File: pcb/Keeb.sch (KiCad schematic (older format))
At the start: 43 parts, among them J1 TRRS_SJ1-42514, J2 TRRS_SJ1-42514, SW1 SW_RST, U1 ATMEGA32U4, U2 PI6ULS5V9511AWEX_I2C_HotSwap, U3 MCP23017_SO, X1 XTAL_GND

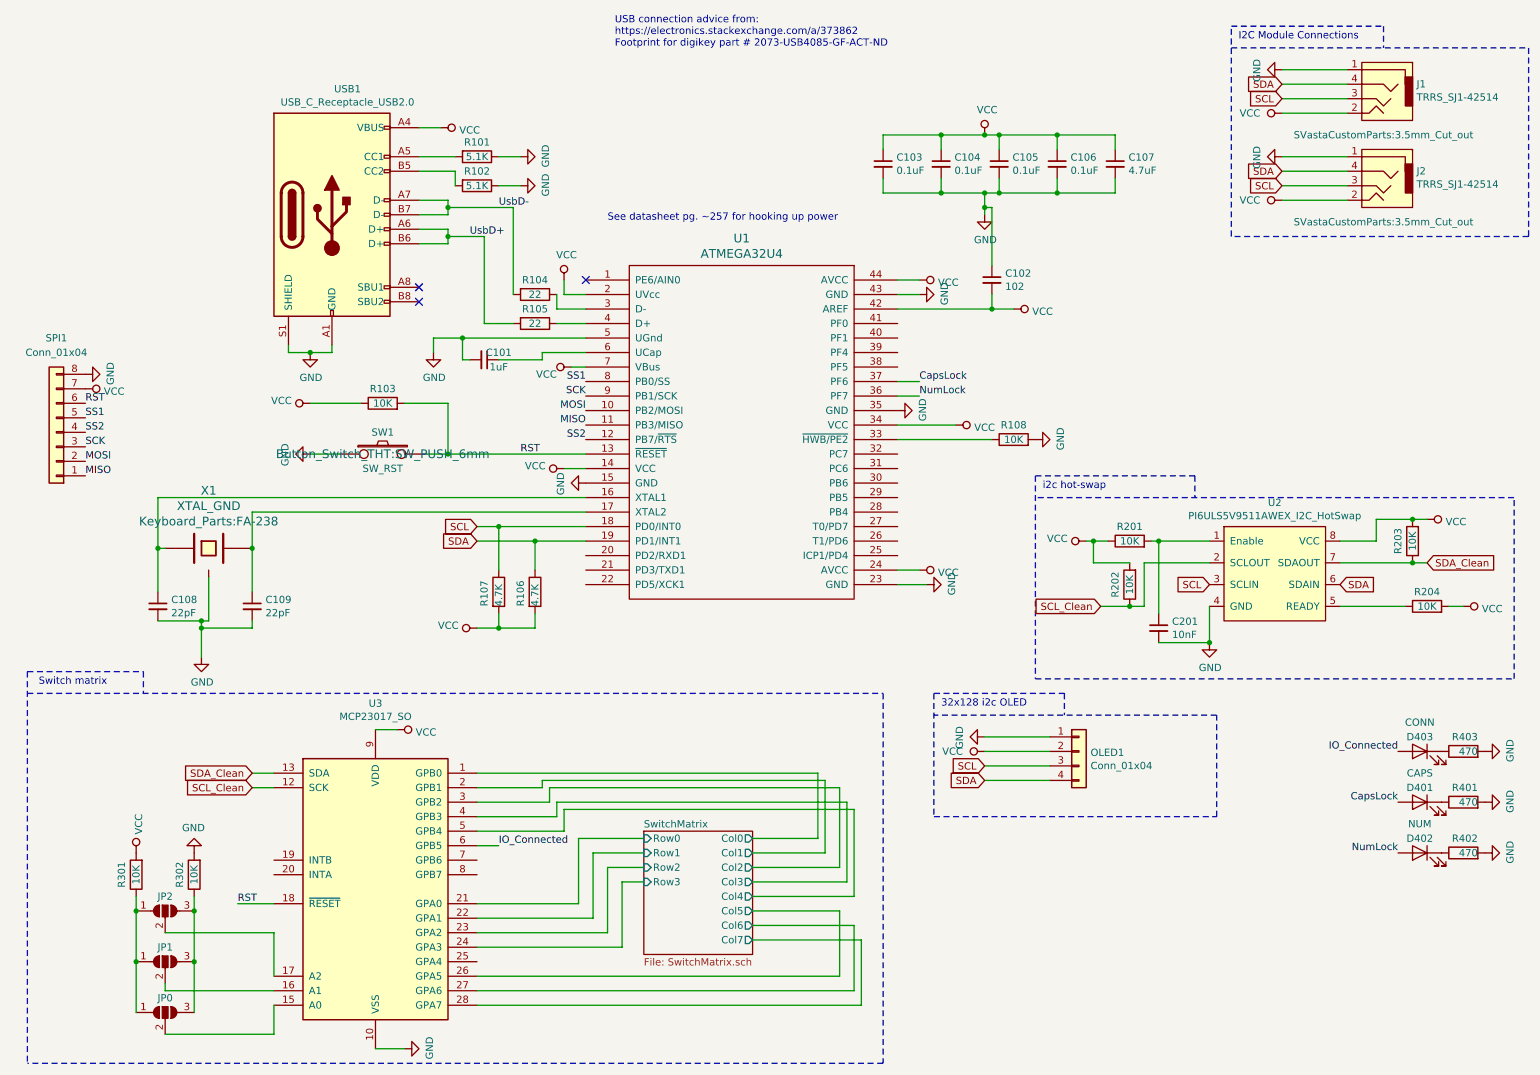
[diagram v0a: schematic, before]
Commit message: Removed most keys to prepare for test PCB
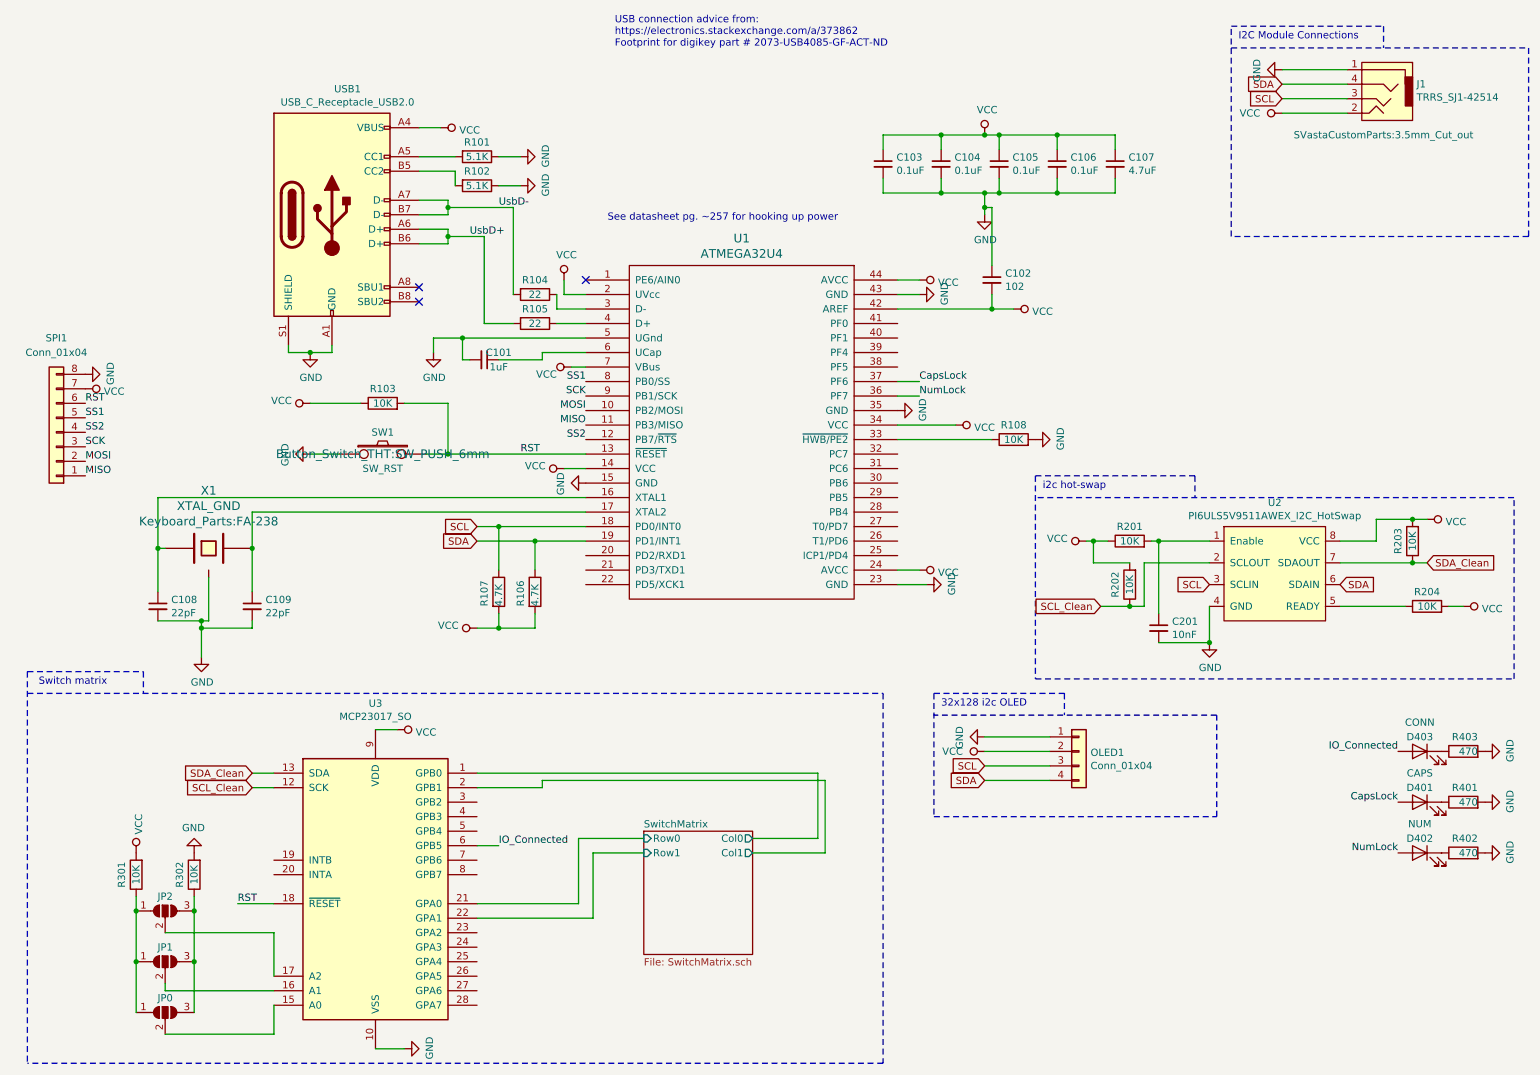
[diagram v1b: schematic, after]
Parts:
- removed J2: TRRS_SJ1-42514, SVastaCustomParts:3.5mm_Cut_out, symbol Keeb-rescue:TRRS_SJ1-42514-SVastaCustomParts-Keeb-rescue
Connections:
- net SwitchMatrix/Col2: no longer names the net of U3.3 (GPB2)
- net SwitchMatrix/Col3: no longer names the net of U3.4 (GPB3)
- net SwitchMatrix/Col4: no longer names the net of U3.5 (GPB4)
- net SwitchMatrix/Col5: no longer names the net of U3.26 (GPA5)
- net SwitchMatrix/Col6: no longer names the net of U3.27 (GPA6)
- net SwitchMatrix/Col7: no longer names the net of U3.28 (GPA7)
- net SwitchMatrix/Row2: no longer names the net of U3.23 (GPA2)
- net SwitchMatrix/Row3: no longer names the net of U3.24 (GPA3)
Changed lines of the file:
@@
 F1 "SwitchMatrix.sch" 50
 F2 "Row0" I L 4950 6200 50
-F3 "Col7" O R 5700 6900 50
-F4 "Row1" I L 4950 6300 50
-F5 "Row2" I L 4950 6400 50
-F6 "Row3" I L 4950 6500 50
-F7 "Col0" O R 5700 6200 50
-F8 "Col1" O R 5700 6300 50
-F9 "Col2" O R 5700 6400 50
-F10 "Col3" O R 5700 6500 50
-F11 "Col4" O R 5700 6600 50
-F12 "Col5" O R 5700 6700 50
-F13 "Col6" O R 5700 6800 50
+F3 "Row1" I L 4950 6300 50
+F4 "Col0" O R 5700 6200 50
+F5 "Col1" O R 5700 6300 50
 $EndSheet
 $Comp
@@
 	700  5200 6600 5200
 Wire Wire Line
-	3800 7350 6450 7350
-Wire Wire Line
-	6450 7350 6450 6900
-Wire Wire Line
-	5700 6900 6450 6900
-Wire Wire Line
-	5700 6800 6400 6800
-Wire Wire Line
-	6400 6800 6400 7250
-Wire Wire Line
-	6400 7250 3800 7250
-Wire Wire Line
-	3800 7150 6300 7150
-Wire Wire Line
-	6300 7150 6300 6700
-Wire Wire Line
-	6300 6700 5700 6700
-Wire Wire Line
 	3800 6650 4500 6650
 Wire Wire Line
@@
 Wire Wire Line
 	4600 6300 4950 6300
-Wire Wire Line
-	3800 6850 4700 6850
-Wire Wire Line
-	4700 6850 4700 6400
-Wire Wire Line
-	4700 6400 4950 6400
-Wire Wire Line
-	3800 6950 4800 6950
-Wire Wire Line
-	4800 6950 4800 6500
-Wire Wire Line
-	4800 6500 4950 6500
 Wire Wire Line
 	6700 3050 6850 3050
@@
 	0    -1   -1   0
 $EndComp
-Text GLabel 9350 1700 0    50   Input ~ 0
-SCL
-$Comp
-L Keeb-rescue:TRRS_SJ1-42514-SVastaCustomParts-Keeb-rescue J2
-U 1 1 5F1C218A
-P 10050 1350
-F 0 "J2" H 9822 1101 50  0000 R CNN
-F 1 "TRRS_SJ1-42514" H 9822 1010 50  0000 R CNN
-F 2 "SVastaCustomParts:3.5mm_Cut_out" H 10050 750 50  0000 C CNN
-F 3 "https://www.cui.com/product/resource/sj1-4251x-series.pdf" H 10050 1350 50  0001 C CNN
-	1    10050 1350
-	-1   0    0    -1
-$EndComp
-Text GLabel 9350 1600 0    50   Input ~ 0
-SDA
-Wire Wire Line
-	9350 1500 9800 1500
-Wire Wire Line
-	9350 1600 9800 1600
-Wire Wire Line
-	9350 1700 9800 1700
 Wire Notes Line
 	11050 750  11050 2050
@@
 F 3 "" H 9350 900 50  0001 C CNN
 	1    9350 900
-	0    1    1    0
-$EndComp
-$Comp
-L power:GND #PWR0114
-U 1 1 5F39B361
-P 9350 1500
-F 0 "#PWR0114" H 9350 1250 50  0001 C CNN
-F 1 "GND" H 9355 1327 50  0000 C CNN
-F 2 "" H 9350 1500 50  0001 C CNN
-F 3 "" H 9350 1500 50  0001 C CNN
-	1    9350 1500
 	0    1    1    0
 $EndComp
@@
 Text Notes 7700 3800 0    50   ~ 0
 i2c hot-swap
-Wire Wire Line
-	3800 6150 4400 6150
-Wire Wire Line
-	4400 6150 4400 6000
-Wire Wire Line
-	4400 6000 6400 6000
-Wire Wire Line
-	6400 6000 6400 6600
-Wire Wire Line
-	6400 6600 5700 6600
-Wire Wire Line
-	3800 6050 4350 6050
-Wire Wire Line
-	4350 6050 4350 5950
-Wire Wire Line
-	4350 5950 6350 5950
-Wire Wire Line
-	6350 5950 6350 6500
-Wire Wire Line
-	6350 6500 5700 6500
-Wire Wire Line
-	3800 5950 4300 5950
-Wire Wire Line
-	4300 5950 4300 5850
-Wire Wire Line
-	4300 5850 6300 5850
-Wire Wire Line
-	6300 5850 6300 6400
-Wire Wire Line
-	6300 6400 5700 6400
 Wire Wire Line
 	3800 5850 4250 5850
@@
 Text Label 1100 3200 0    50   ~ 0
 RST
-Wire Wire Line
-	9350 1800 9800 1800
-$Comp
-L power:VCC #PWR010
-U 1 1 5F1C2196
-P 9350 1800
-F 0 "#PWR010" H 9350 1650 50  0001 C CNN
-F 1 "VCC" V 9350 1950 50  0000 L CNN
-F 2 "" H 9350 1800 50  0001 C CNN
-F 3 "" H 9350 1800 50  0001 C CNN
-	1    9350 1800
-	0    -1   -1   0
-$EndComp
 $EndSCHEMATC

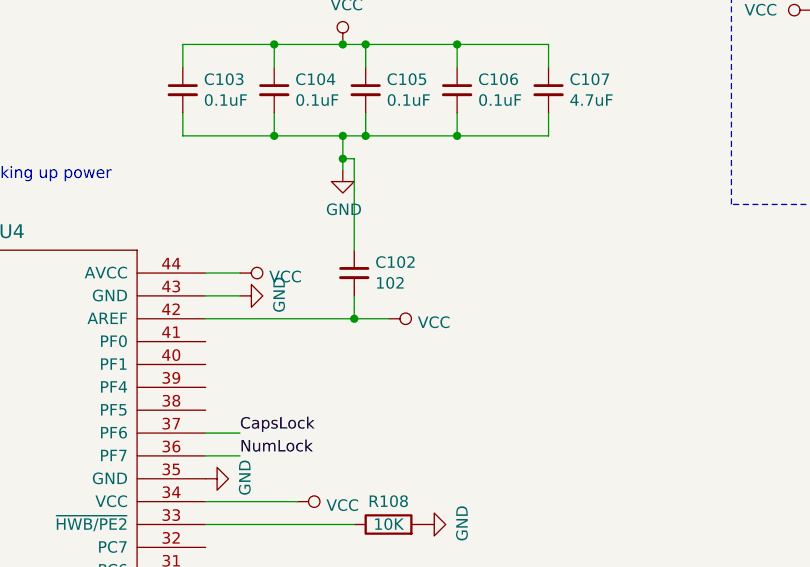
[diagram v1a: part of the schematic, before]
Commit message: Disabled keebio library
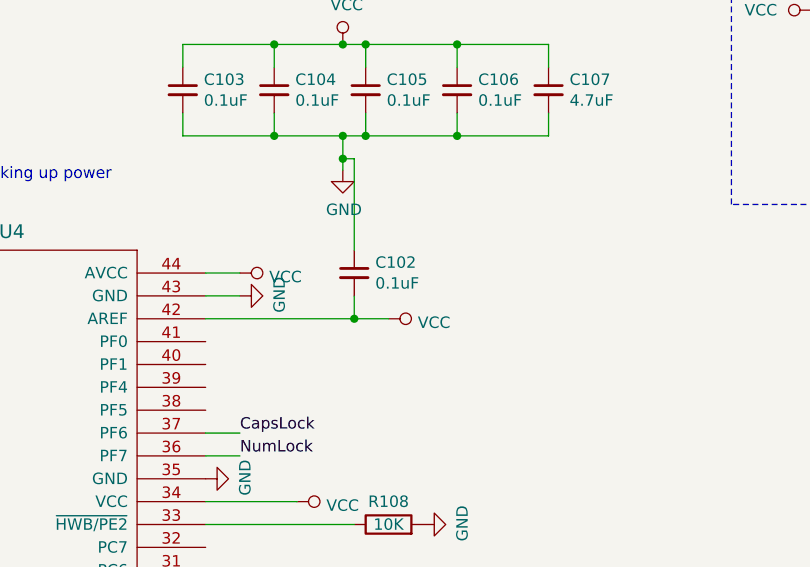
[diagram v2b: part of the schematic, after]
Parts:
- C102: value 102 -> 0.1uF
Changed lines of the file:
@@
 P 7350 2350
 F 0 "C102" H 7442 2396 50  0000 L CNN
-F 1 "102" H 7442 2305 50  0000 L CNN
+F 1 "0.1uF" H 7442 2305 50  0000 L CNN
 F 2 "Capacitor_SMD:C_0805_2012Metric_Pad1.15x1.40mm_HandSolder" H 7350 2350 50  0001 C CNN
 F 3 "~" H 7350 2350 50  0001 C CNN
